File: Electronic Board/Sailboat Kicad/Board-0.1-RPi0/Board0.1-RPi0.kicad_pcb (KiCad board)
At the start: 2 copper layers, 51.4 x 65.4 mm, 26 parts, among them J1 Conn_02x20_Odd_Even, J10 Conn_01x03, J11 Conn_01x03, J12 Conn_01x03, J2 Conn_02x12_Odd_Even, J3 Conn_01x01, J4 Conn_02x12_Odd_Even, J5 Conn_01x01, J6 Conn_02x12_Odd_Even, J7 Conn_01x02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

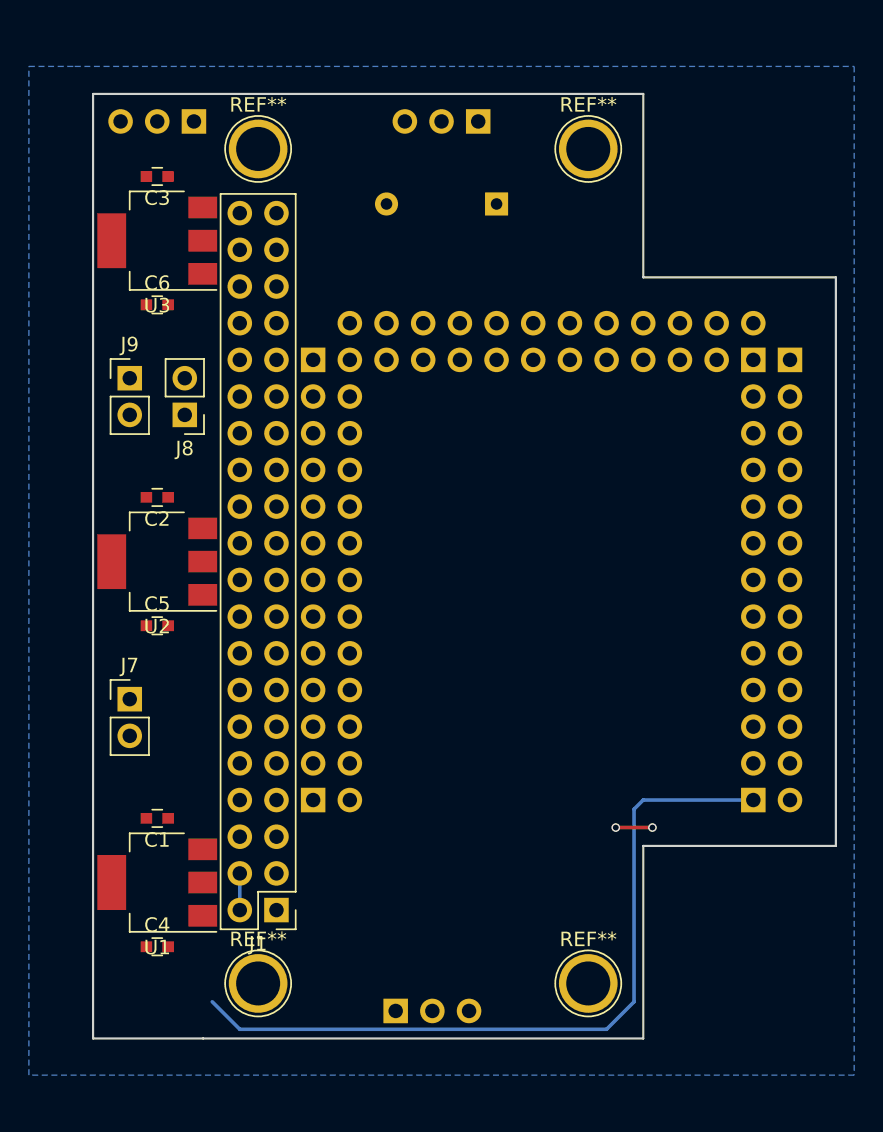
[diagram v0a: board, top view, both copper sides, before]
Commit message: Removed the arduino. Why keep it?? Doesn't make sense :/
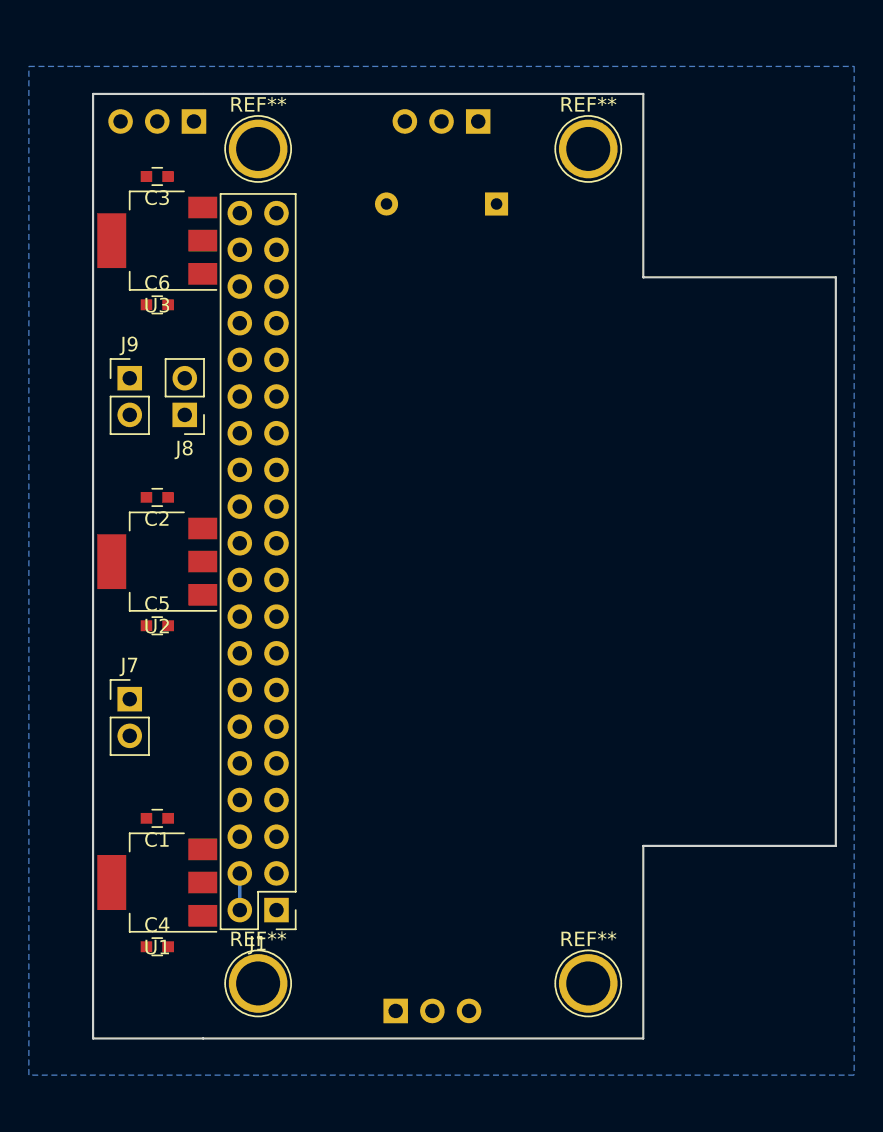
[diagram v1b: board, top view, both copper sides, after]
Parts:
- removed J2, J4, J6: Conn_02x12_Odd_Even, Pin_Headers:Pin_Header_Straight_2x12_Pitch2.54mm
- removed J3, J5: Conn_01x01, Pin_Headers:Pin_Header_Straight_1x01_Pitch2.54mm
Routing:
- net +5V: track 55.2 -> 2.54 mm
- net (no net): track 2.54 -> 0.00 mm, vias 2 -> 0

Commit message: Components installed for a working rpi0 shield for sailboat
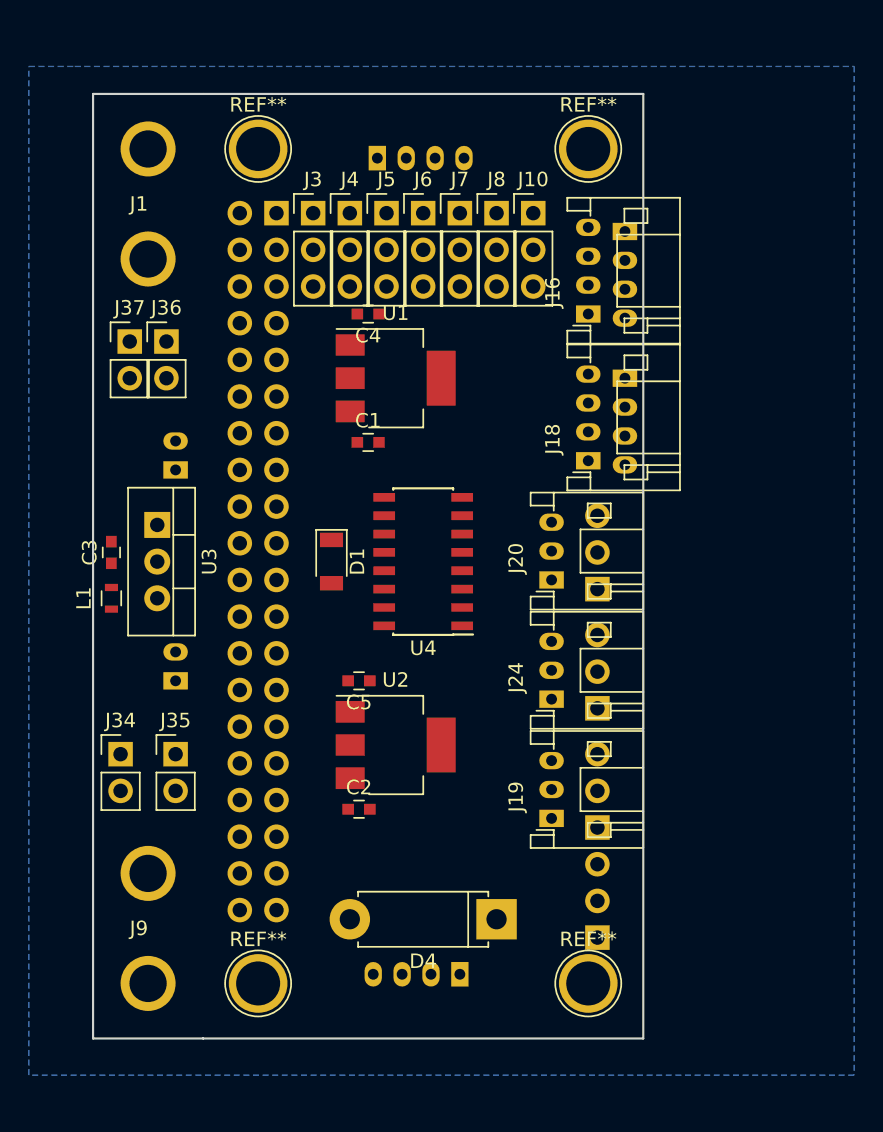
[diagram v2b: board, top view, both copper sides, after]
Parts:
- removed C6: 10uF, Capacitors_SMD:C_0603
- removed SW1: SW_DIP_x01, Buttons_Switches_THT:SW_DIP_x1_W7.62mm_Slide
- added D1: D_Schottky_Small, Diodes_SMD:D_1206, F.Cu at (92.7, 76.2)
- added D4: D_Schottky, Diodes_THT:D_5W_P10.16mm_Horizontal, F.Cu at (104.1, 101.0)
- added J13: Conn_01x03_Male, Pin_Headers:Pin_Header_Angled_1x03_Pitch2.54mm, B.Cu at (111.1, 94.6)
- added J14: Conn_01x03_Male, Pin_Headers:Pin_Header_Angled_1x03_Pitch2.54mm, B.Cu at (111.1, 102.2)
- added J15: Conn_01x04, Connectors_JST:JST_PH_S4B-PH-K_04x2.00mm_Angled, B.Cu at (113.0, 63.5)
- added J16: Conn_01x04, Connectors_JST:JST_PH_S4B-PH-K_04x2.00mm_Angled, F.Cu at (110.5, 59.1)
- added J17: Conn_01x04, Connectors_JST:JST_PH_S4B-PH-K_04x2.00mm_Angled, B.Cu at (113.0, 53.3)
- added J18: Conn_01x04, Connectors_JST:JST_PH_S4B-PH-K_04x2.00mm_Angled, F.Cu at (110.5, 69.2)
- added J19: Conn_01x03, Connectors_JST:JST_PH_S3B-PH-K_03x2.00mm_Angled, F.Cu at (108.0, 94.0)
- added J2: Conn_02x20_Odd_Even, Pin_Headers:Pin_Header_Straight_2x20_Pitch2.54mm, B.Cu at (88.9, 52.1)
- added J20: Conn_01x03, Connectors_JST:JST_PH_S3B-PH-K_03x2.00mm_Angled, F.Cu at (108.0, 77.5)
- added J21: Conn_01x02, Connectors_JST:JST_PH_S2B-PH-K_02x2.00mm_Angled, B.Cu at (81.9, 84.5)
- added J22: Conn_01x02, Connectors_JST:JST_PH_S2B-PH-K_02x2.00mm_Angled, B.Cu at (81.9, 69.8)
- added J24: Conn_01x03, Connectors_JST:JST_PH_S3B-PH-K_03x2.00mm_Angled, F.Cu at (108.0, 85.7)
- added J3: Conn_01x03, Pin_Headers:Pin_Header_Straight_1x03_Pitch2.54mm, F.Cu at (91.4, 52.1)
- added J31: Conn_01x04, Connectors_JST:JST_PH_S4B-PH-K_04x2.00mm_Angled, B.Cu at (95.9, 48.3)
- added J32: Conn_01x04, Connectors_JST:JST_PH_S4B-PH-K_04x2.00mm_Angled, B.Cu at (101.6, 104.8)
- added J34: Conn_01x02, Pin_Headers:Pin_Header_Straight_1x02_Pitch2.54mm, F.Cu at (78.1, 89.5)
- added J35: Conn_01x02, Pin_Headers:Pin_Header_Straight_1x02_Pitch2.54mm, F.Cu at (81.9, 89.5)
- added J36: Conn_01x02, Pin_Headers:Pin_Header_Straight_1x02_Pitch2.54mm, F.Cu at (81.3, 61.0)
- added J37: Conn_01x02, Pin_Headers:Pin_Header_Straight_1x02_Pitch2.54mm, F.Cu at (78.7, 61.0)
- added J4: Conn_01x03, Pin_Headers:Pin_Header_Straight_1x03_Pitch2.54mm, F.Cu at (94.0, 52.1)
- added J5: Conn_01x03, Pin_Headers:Pin_Header_Straight_1x03_Pitch2.54mm, F.Cu at (96.5, 52.1)
- added J6: Conn_01x03, Pin_Headers:Pin_Header_Straight_1x03_Pitch2.54mm, F.Cu at (99.1, 52.1)
- added L1: 3.3uH, Inductors_SMD:L_0603, F.Cu at (77.5, 78.7)
- added U4: MCP3008, Housings_SOIC:SOIC-16_3.9x9.9mm_Pitch1.27mm, F.Cu at (99.1, 76.2)
- C3: value 100nF -> 0.33uF
- J1: value Conn_02x20_Odd_Even -> Conn_01x02; footprint Pin_Headers:Pin_Header_Straight_2x20_Pitch2.54mm -> Sailboat:BAT-CONN
- J10: moved to F.Cu
- J11, J12: value Conn_01x03 -> Conn_01x03_Male
- J7, J8: value Conn_01x02 -> Conn_01x03; footprint Pin_Headers:Pin_Header_Straight_1x02_Pitch2.54mm -> Pin_Headers:Pin_Header_Straight_1x03_Pitch2.54mm
- J9: footprint Pin_Headers:Pin_Header_Straight_1x02_Pitch2.54mm -> Sailboat:BAT-CONN
- U3: value LD1117S50TR_SOT223 -> L7805; footprint TO_SOT_Packages_SMD:SOT-223-3_TabPin2 -> TO_SOT_Packages_THT:TO-220-3_Vertical
- moved REF** 57.8 mm to (110.5, 105.4)
- moved REF** 57.8 mm to (87.6, 105.4)
- moved REF** 57.8 mm to (87.6, 47.6)
- moved REF** 57.8 mm to (110.5, 47.6)
- moved J1 49.7 mm to (80.0, 51.4), turned to 0 degrees
- moved C4 46.2 mm to (95.2, 59.1), turned to 180 degrees
- moved J12 41.5 mm to (111.1, 86.4), turned to 0 degrees
- moved J7 40.7 mm to (101.6, 52.1)
- moved U1 38.6 mm to (97.2, 63.5), turned to 0 degrees
- moved J9 38.1 mm to (80.0, 101.6)
- moved J11 32.4 mm to (111.1, 78.1), turned to 0 degrees
- moved C1 29.9 mm to (95.2, 67.9), turned to 0 degrees
- moved C3 26.2 mm to (77.5, 75.6), turned to 90 degrees
- moved J8 25.7 mm to (104.1, 52.1), turned to 0 degrees
- moved C2 25.7 mm to (94.6, 93.3), turned to 0 degrees
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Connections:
- C5 pad 1: +5VP -> +5VA
- J1 pad 2: +5V -> Net-(J1-Pad2)
- J10 pad 1: BAT1- -> GND
- J10 pad 2: GND -> +5VA
- J10 pad 3: BAT2- -> Net-(J10-Pad3)
- J11 pad 1: GND -> GPIO5
- J11 pad 3: servo1 -> GND
- J12 pad 1: GND -> GPIO6
- J12 pad 3: servo2 -> GND
- J7 pad 1: BAT1+ -> GND
- J7 pad 2: BAT1- -> Net-(J7-Pad2)
- J8 pad 1: BAT1- -> GND
- J8 pad 2: BAT2+ -> Net-(J8-Pad2)
- J9 pad 1: BAT2+ -> GND
- J9 pad 2: BAT2- -> Net-(D4-Pad1)
- U2 pad 2: +5VP -> +5VA
- U3 pad 1: GND -> Net-(D1-Pad1)
- U3 pad 2: +5VD -> GND
- U3 pad 3: BAT+ -> +5VP
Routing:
- net +5V: track 2.54 -> 0.00 mm
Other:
- board size 51.4 x 65.4 mm -> 38.1 x 65.4 mm

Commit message: Finished tracing the RPi0 Board and plotted the gerbers, ready for production
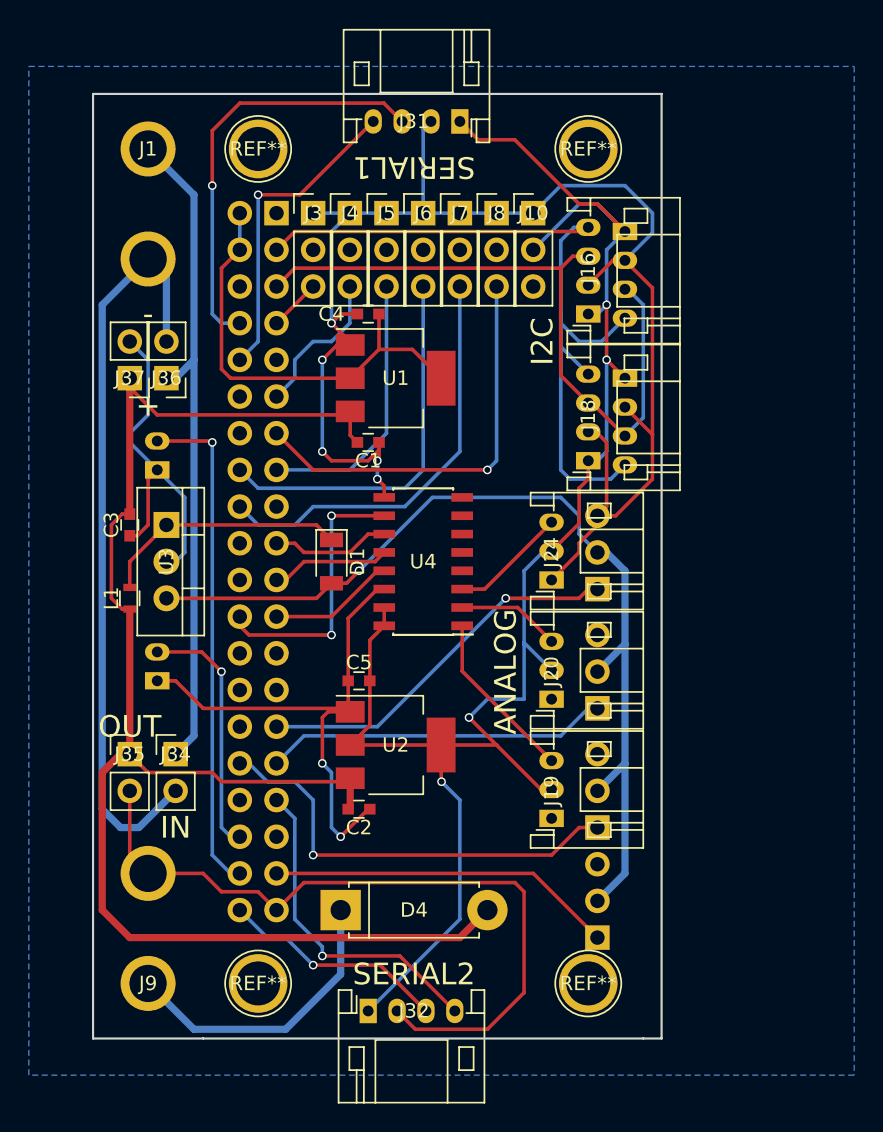
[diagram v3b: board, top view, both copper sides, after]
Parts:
- J31, J32: moved to F.Cu
- moved D4 10.8 mm to (93.3, 100.3), turned to 0 degrees
- moved J20 8.25 mm to (108.0, 85.7)
- moved J24 8.25 mm to (108.0, 77.5)
- moved J32 6.84 mm to (95.2, 107.3), turned to 0 degrees
- moved J31 6.25 mm to (101.6, 45.7), turned to 180 degrees
- moved J34 3.81 mm to (81.9, 89.5)
- moved J35 3.18 mm to (78.7, 89.5)
- moved J36 2.54 mm to (81.3, 63.5), turned to 180 degrees
- moved J37 2.54 mm to (78.7, 63.5), turned to 180 degrees
- moved C3 2.29 mm to (78.7, 73.7), turned to 270 degrees
- moved J21 1.27 mm to (80.6, 84.5)
- moved J22 1.27 mm to (80.6, 69.8)
- moved L1 1.27 mm to (78.7, 78.7), turned to 270 degrees
- moved U3 0.64 mm to (81.3, 73.7)
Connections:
- J2 pad 16: TX1 -> GPIO21
- J2 pad 18: RX1 -> GPIO13
- J2 pad 33: GPIO13 -> RX1
- J2 pad 40: GPIO21 -> TX1
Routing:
- net GND: track 0.00 -> 218.6 mm, vias 0 -> 7
- net +5VA: track 0.00 -> 119.5 mm, vias 0 -> 4
- net BAT+: track 0.00 -> 105.4 mm
- net +5VP: track 0.00 -> 67.2 mm, vias 0 -> 1
- net SDA: track 0.00 -> 54.5 mm
- net Net-(J1-Pad2): track 0.00 -> 52.3 mm
- net SCL: track 0.00 -> 47.6 mm
- net Net-(J1-Pad1): track 0.00 -> 46.2 mm
- net GPIO20: track 0.00 -> 34.9 mm, vias 0 -> 1
- net +5V: track 0.00 -> 30.9 mm
- net GPIO12: track 0.00 -> 30.4 mm, vias 0 -> 1
- net TX0: track 0.00 -> 29.3 mm, vias 0 -> 1
- net GPIO13: track 0.00 -> 29.3 mm
- net GPIO27: track 0.00 -> 28.6 mm, vias 0 -> 1
- net GPIO21: track 0.00 -> 26.5 mm
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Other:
- board size 38.1 x 65.4 mm -> 39.4 x 65.4 mm
- board text added: "+"
- board text added: "-"
- board text added: "ANALOG"
- board text added: "D1"
- board text added: "D2"
- board text added: "I2C"
- board text added: "IN"
- board text added: "OUT"
- board text added: "S-1"
- board text added: "S-2"
- board text added: "S-3"
- board text added: "S-4"
- board text added: "SERIAL1"
- board text added: "SERIAL2"
